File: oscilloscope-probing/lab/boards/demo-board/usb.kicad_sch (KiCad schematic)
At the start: 14 parts, among them J14 USB_C_Receptacle_USB2.0, U1 FT234XD, U39 NCP45525IMNTWG-H

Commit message: Finished initial demo board schematic
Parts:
- added R51, R52: 0, symbol device:R
- added TP10, TP11: TESTCLIP, symbol conn:CONN_01X01
- added TP13: CONN_01X03, symbol conn:CONN_01X03
- J14: footprint lain:GCT_USB4500-03-0-A -> Connector_USB:USB_C_Receptacle_HRO_TYPE-C-31-M-12
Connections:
- net GND: now also TP13.3 (P3)
- net UART_RX: now also TP13.2 (P2)
- net UART_TX: now also TP13.1 (P1)
- net USB_D_N: now also R52.1
- net USB_D_P: now also R51.1
- new net: R51.2, TP11.1 (P1)
- new net: R52.2, TP10.1 (P1)
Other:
- note added: "Test points for USB protocol decode"

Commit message: Continued initial schematic, assigned footprints
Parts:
- C1: footprint (none) -> azonenberg_pcb:EIA_0603_CAP_NOSILK
- C2, C3: footprint (none) -> azonenberg_pcb:EIA_0402_CAP_NOSILK
- J14: footprint Connector_USB:USB_C_Receptacle_HRO_TYPE-C-31-M-12 -> lain:GCT_USB4500-03-0-A
- R1, R2, R51, R52: footprint (none) -> azonenberg_pcb:EIA_0402_RES_NOSILK
- TP10, TP11: footprint (none) -> azonenberg_pcb:TESTPOINT_SMT_KEYSTONE_5016
- TP13: footprint (none) -> azonenberg_pcb:CONN_HEADER_2.54MM_1x3_REFLOW
- U1: footprint (none) -> azonenberg_pcb:DFN_12_0.5MM_3x3MM
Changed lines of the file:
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@@
 			)
 		)
-		(property "Footprint" ""
+		(property "Footprint" "azonenberg_pcb:TESTPOINT_SMT_KEYSTONE_5016"
 			(at 41.91 144.78 0)
 			(effects
@@
 			)
 		)
-		(property "Footprint" ""
+		(property "Footprint" "azonenberg_pcb:EIA_0402_RES_NOSILK"
 			(at 33.02 152.908 90)
 			(effects
@@
 			)
 		)
-		(property "Footprint" ""
+		(property "Footprint" "azonenberg_pcb:EIA_0402_RES_NOSILK"
 			(at 55.88 47.498 90)
 			(effects
@@
 			)
 		)
-		(property "Footprint" ""
+		(property "Footprint" "azonenberg_pcb:EIA_0402_RES_NOSILK"
 			(at 33.02 146.558 90)
 			(effects
@@
 			)
 		)
-		(property "Footprint" ""
+		(property "Footprint" "azonenberg_pcb:TESTPOINT_SMT_KEYSTONE_5016"
 			(at 41.91 151.13 0)
 			(effects
@@
 			)
 		)
-		(property "Footprint" "Connector_USB:USB_C_Receptacle_HRO_TYPE-C-31-M-12"
+		(property "Footprint" "lain:GCT_USB4500-03-0-A"
 			(at 40.64 43.18 0)
 			(effects
@@
 			)
 		)
-		(property "Footprint" ""
+		(property "Footprint" "azonenberg_pcb:EIA_0402_CAP_NOSILK"
 			(at 75.8952 99.06 0)
 			(effects
@@
 			)
 		)
-		(property "Footprint" ""
+		(property "Footprint" "azonenberg_pcb:DFN_12_0.5MM_3x3MM"
 			(at 26.67 107.95 0)
 			(effects
@@
 			)
 		)
-		(property "Footprint" ""
+		(property "Footprint" "azonenberg_pcb:EIA_0603_CAP_NOSILK"
 			(at 75.8952 87.63 0)
 			(effects
@@
 			)
 		)
-		(property "Footprint" ""
+		(property "Footprint" "azonenberg_pcb:EIA_0402_RES_NOSILK"
 			(at 55.88 42.418 90)
 			(effects
@@
 			)
 		)
-		(property "Footprint" ""
+		(property "Footprint" "azonenberg_pcb:CONN_HEADER_2.54MM_1x3_REFLOW"
 			(at 41.91 162.56 0)
 			(effects
@@
 			)
 		)
-		(property "Footprint" ""
+		(property "Footprint" "azonenberg_pcb:EIA_0402_CAP_NOSILK"
 			(at 89.8652 87.63 0)
 			(effects

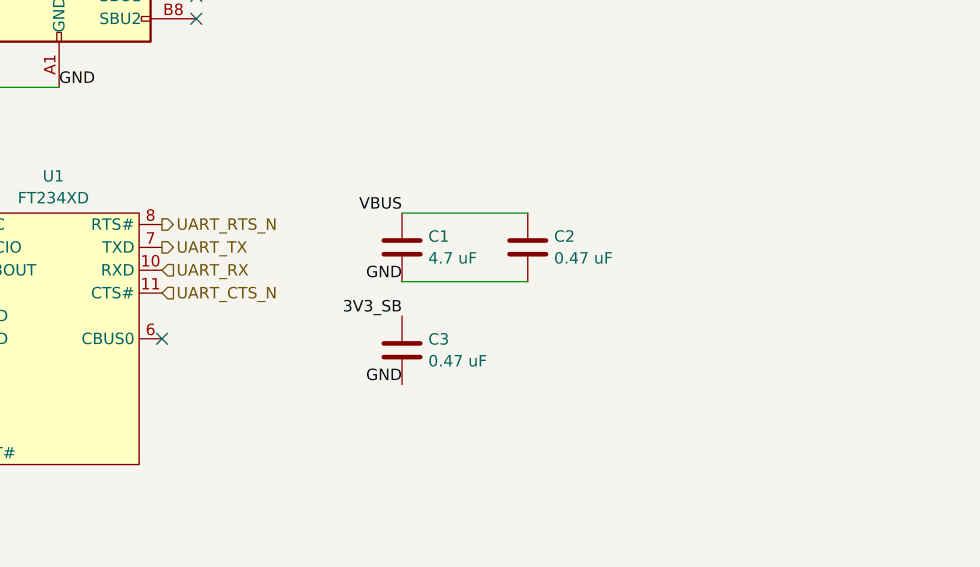
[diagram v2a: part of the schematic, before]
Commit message: Continued demo board layout
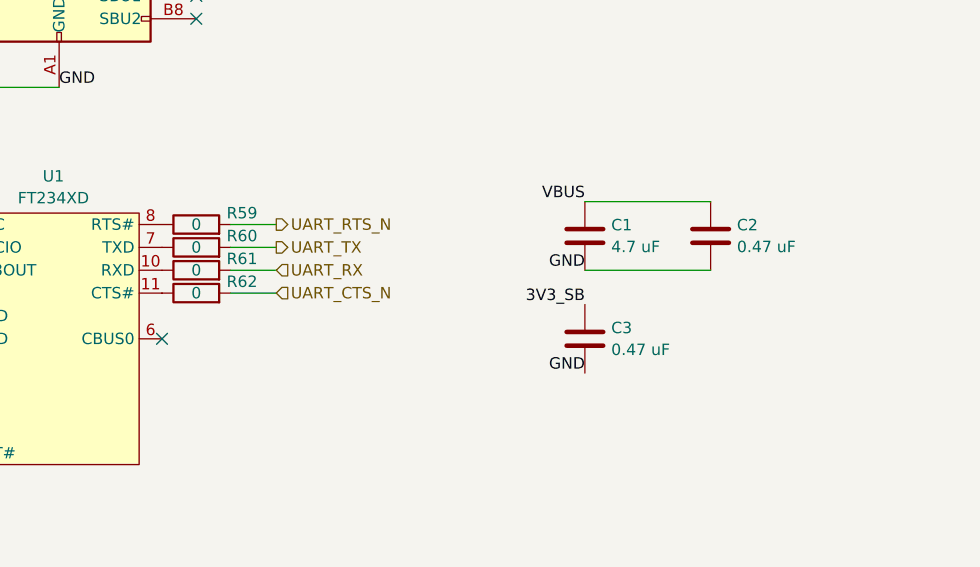
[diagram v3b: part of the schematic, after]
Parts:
- added R59, R60, R61, R62: 0, azonenberg_pcb:EIA_0402_RES_NOSILK, symbol device:R
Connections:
- net UART_CTS_N: now also R62.2; no longer U1.11 (CTS#)
- net UART_RTS_N: now also R59.2; no longer U1.8 (RTS#)
- net UART_RX: now also R61.2; no longer U1.10 (RXD)
- net UART_TX: now also R60.2; no longer U1.7 (TXD)
- new net: R62.1, U1.11 (CTS#)
- new net: R59.1, U1.8 (RTS#)
- new net: R61.1, U1.10 (RXD)
- new net: R60.1, U1.7 (TXD)
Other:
- moved on the sheet: C1, C2, C3

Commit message: Continued demo board layout
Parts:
- added TP18, TP19: TESTCLIP, azonenberg_pcb:TESTPOINT_SMT_KEYSTONE_5016, symbol conn:CONN_01X01
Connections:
- net GND: now also TP18.1 (P1), TP19.1 (P1)
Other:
- company: (none) -> Antikernel Labs
- title: (none) -> Probing Demo Board
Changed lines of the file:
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@@
 	(generator_version "9.0")
 	(paper "A4")
+	(title_block
+		(title "Probing Demo Board")
+		(date "2026-08-06")
+		(rev "0.1")
+		(company "Antikernel Labs")
+		(comment 1 "Andrew D. Zonenberg")
+	)
 	(text "Test points for USB protocol decode"
 		(exclude_from_sim no)
@@
 		)
 	)
+	(label "GND"
+		(at 72.39 144.78 180)
+		(effects
+			(font
+				(size 1.27 1.27)
+			)
+			(justify right bottom)
+		)
+	)
 	(label "VBUS_RAW"
 		(at 107.95 45.72 180)
@@
 			)
 			(justify left bottom)
+		)
+	)
+	(label "GND"
+		(at 72.39 151.13 180)
+		(effects
+			(font
+				(size 1.27 1.27)
+			)
+			(justify right bottom)
 		)
 	)
@@
 			)
 			(justify left)
+		)
+	)
+	(symbol
+		(lib_id "conn:CONN_01X01")
+		(at 77.47 151.13 0)
+		(unit 1)
+		(exclude_from_sim no)
+		(in_bom yes)
+		(on_board yes)
+		(dnp no)
+		(fields_autoplaced yes)
+		(property "Reference" "TP19"
+			(at 79.375 149.9178 0)
+			(effects
+				(font
+					(size 1.27 1.27)
+				)
+				(justify left)
+			)
+		)
+		(property "Value" "TESTCLIP"
+			(at 79.375 152.3421 0)
+			(effects
+				(font
+					(size 1.27 1.27)
+				)
+				(justify left)
+			)
+		)
+		(property "Footprint" "azonenberg_pcb:TESTPOINT_SMT_KEYSTONE_5016"
+			(at 77.47 151.13 0)
+			(effects
+				(font
+					(size 1.27 1.27)
+				)
+				(hide yes)
+			)
+		)
+		(property "Datasheet" ""
+			(at 77.47 151.13 0)
+			(effects
+				(font
+					(size 1.27 1.27)
+				)
+				(hide yes)
+			)
+		)
+		(property "Description" "Connector, single row, 01x01, pin header"
+			(at 77.47 151.13 0)
+			(effects
+				(font
+					(size 1.27 1.27)
+				)
+				(hide yes)
+			)
+		)
+		(pin "1"
+		)
+		(instances
+			(project "demo-board"
+				(path "/aa2d82c6-7ba7-4266-9b47-ed3339e6c556/c8f34d2e-868d-481d-b747-85b27fae8b71"
+					(reference "TP19")
+					(unit 1)
+				)
+			)
 		)
 	)
@@
 					(unit 1)
 				)
+			)
+		)
+	)
+	(symbol
+		(lib_id "conn:CONN_01X01")
+		(at 77.47 144.78 0)
+		(unit 1)
+		(exclude_from_sim no)
+		(in_bom yes)
+		(on_board yes)
+		(dnp no)
+		(fields_autoplaced yes)
+		(property "Reference" "TP18"
+			(at 79.375 143.5678 0)
+			(effects
+				(font
+					(size 1.27 1.27)
+				)
+				(justify left)
+			)
+		)
+		(property "Value" "TESTCLIP"
+			(at 79.375 145.9921 0)
+			(effects
+				(font
+					(size 1.27 1.27)
+				)
+				(justify left)
+			)
+		)
+		(property "Footprint" "azonenberg_pcb:TESTPOINT_SMT_KEYSTONE_5016"
+			(at 77.47 144.78 0)
+			(effects
+				(font
+					(size 1.27 1.27)
+				)
+				(hide yes)
+			)
+		)
+		(property "Datasheet" ""
+			(at 77.47 144.78 0)
+			(effects
+				(font
+					(size 1.27 1.27)
+				)
+				(hide yes)
+			)
+		)
+		(property "Description" "Connector, single row, 01x01, pin header"
+			(at 77.47 144.78 0)
+			(effects
+				(font
+					(size 1.27 1.27)
+				)
+				(hide yes)
+			)
+		)
+		(pin "1"
+		)
+		(instances
+			(project "demo-board"
+				(path "/aa2d82c6-7ba7-4266-9b47-ed3339e6c556/c8f34d2e-868d-481d-b747-85b27fae8b71"
+					(reference "TP18")
+					(unit 1)
+				)

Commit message: Continued demo board layout
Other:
- title: Probing Demo Board -> Oscilloscope Demo Board
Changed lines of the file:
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@@
 	(paper "A4")
 	(title_block
-		(title "Probing Demo Board")
-		(date "2026-08-06")
+		(title "Oscilloscope Demo Board")
+		(date "2026-08-08")
 		(rev "0.1")
 		(company "Antikernel Labs")
